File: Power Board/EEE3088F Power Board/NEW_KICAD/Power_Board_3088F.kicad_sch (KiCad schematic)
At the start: 92 parts, among them J1 Conn_02x16_Odd_Even, J2 USB_C_Receptacle, J3 Conn_01x02_Socket, Q1 2N7002, U1 INA219AIDCNR, U10 DRV8837DSGR, U11 DRV8837DSGR, U12 DRV8837DSGR, U13 DRV8837DSGR, U2 TPS5430DDA, U3 TP4056-42-ESOP8, U7 AP22966DC8-7, U9 CH224K

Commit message: finished schematic
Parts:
- removed C_B1, C_B2: 10uF, Capacitor_SMD:C_0603_1608Metric_Pad1.08x0.95mm_HandSolder, symbol Device:C
- removed C_B3: 220uF, Capacitor_SMD:CP_Elec_6.3x7.7, symbol Device:C_Small
- removed C_Bboot1: 10nF, Capacitor_SMD:C_0603_1608Metric_Pad1.08x0.95mm_HandSolder, symbol Device:C_Small
- removed C_Bin1: 10uF, Capacitor_SMD:C_1206_3216Metric_Pad1.33x1.80mm_HandSolder, symbol Device:C_Small
- removed D2: Red LED, LED_SMD:LED_0603_1608Metric_Pad1.05x0.95mm_HandSolder, symbol Device:LED
- removed D3: Green LED, LED_SMD:LED_0805_2012Metric_Pad1.15x1.40mm_HandSolder, symbol Device:LED
- removed D4: BA340A, custom_footprints:SMA-DIODE, symbol Custom_symbols:B340A
- removed J2: USB_C_Receptacle, Connector_USB:USB_C_Receptacle_G-Switch_GT-USB-7010ASV, symbol Connector:USB_C_Receptacle
- removed L1: 18uH, Inductor_SMD:L_Abracon_ASPI-4030S, symbol Device:L_Small
- removed Q1: 2N7002, Package_TO_SOT_SMD:SOT-23, symbol Transistor_FET:2N7002
- removed R19, R20: 1R, Resistor_SMD:R_0603_1608Metric_Pad0.98x0.95mm_HandSolder, symbol Device:R_US
- removed R_B_LED1, R_B_LED2: 1k, Resistor_SMD:R_0603_1608Metric_Pad0.98x0.95mm_HandSolder, symbol Device:R_US
- removed R_B_b1: 100R, Resistor_SMD:R_0603_1608Metric_Pad0.98x0.95mm_HandSolder, symbol Device:R_US
- removed R_B_fast1: 2k7, Resistor_SMD:R_0603_1608Metric_Pad0.98x0.95mm_HandSolder, symbol Device:R_US
- removed R_B_pd1: 10k, Resistor_SMD:R_0603_1608Metric_Pad0.98x0.95mm_HandSolder, symbol Device:R_US
- removed R_B_slow1: 5k6, Resistor_SMD:R_0603_1608Metric_Pad0.98x0.95mm_HandSolder, symbol Device:R_US
- removed R_Bset1: 10k, Resistor_SMD:R_0603_1608Metric_Pad0.98x0.95mm_HandSolder, symbol Device:R_Small_US
- removed R_Bset2: 3k3, Resistor_SMD:R_0603_1608Metric_Pad0.98x0.95mm_HandSolder, symbol Device:R_Small_US
- removed TP10, TP11, TP12, TP13, TP14, TP15, TP17: TestPoint, TestPoint:TestPoint_Pad_D2.0mm, symbol Connector:TestPoint
- removed U1: INA219AIDCNR, Package_TO_SOT_SMD:SOT-23-8, symbol Sensor_Energy:INA219AxDCN
- removed U10, U11, U12, U13: DRV8837DSGR, custom_footprints:SON50P200X200X80-9N, symbol Custom_symbols:DRV8837DSGR
- removed U2: TPS5430DDA, Package_SO:SOIC-8-1EP_3.9x4.9mm_P1.27mm_EP2.29x3mm, symbol Regulator_Switching:TPS5430DDA
- removed U3: TP4056-42-ESOP8, custom_footprints:SOIC127P600X175-9N, symbol Battery_Management:TP4056-42-ESOP8
- added C_B3, C_B5: 10uF, Capacitor_SMD:C_0603_1608Metric_Pad1.08x0.95mm_HandSolder, symbol Device:C
- added C_B4: 220uF, Capacitor_SMD:CP_Elec_6.3x7.7, symbol Device:C_Small
- added C_Bboot2: 10nF, Capacitor_SMD:C_0603_1608Metric_Pad1.08x0.95mm_HandSolder, symbol Device:C_Small
- added C_Bin2: 10uF, Capacitor_SMD:C_1206_3216Metric_Pad1.33x1.80mm_HandSolder, symbol Device:C_Small
- added D4: Red LED, LED_SMD:LED_0603_1608Metric_Pad1.05x0.95mm_HandSolder, symbol Device:LED
- added D7: BA340A, custom_footprints:SMA-DIODE, symbol Custom_symbols:B340A
- added D8: Green LED, LED_SMD:LED_0603_1608Metric_Pad1.05x0.95mm_HandSolder, symbol Device:LED
- added JP_B1: charge_in, Jumper:SolderJumper-2_P1.3mm_Open_RoundedPad1.0x1.5mm, symbol Jumper:SolderJumper_2_Open
- added JP_B2: buck_charge, Jumper:SolderJumper-2_P1.3mm_Open_RoundedPad1.0x1.5mm, symbol Jumper:SolderJumper_2_Open
- added JP_BBatt1: charge_batt+, Jumper:SolderJumper-2_P1.3mm_Open_RoundedPad1.0x1.5mm, symbol Jumper:SolderJumper_2_Open
- added JP_B_ena1: Jumper (leave open), Jumper:SolderJumper-2_P1.3mm_Open_RoundedPad1.0x1.5mm, symbol Jumper:SolderJumper_2_Open
- added JP_Bprog1: fast_prog, Jumper:SolderJumper-2_P1.3mm_Open_RoundedPad1.0x1.5mm, symbol Jumper:SolderJumper_2_Open
- added JP_CVbus1: VBUS, Jumper:SolderJumper-2_P1.3mm_Open_RoundedPad1.0x1.5mm, symbol Jumper:SolderJumper_2_Open
- added JP_M_VM1: Batt_VM, Jumper:SolderJumper-2_P1.3mm_Open_RoundedPad1.0x1.5mm, symbol Jumper:SolderJumper_2_Open
- added JP_P1: Boost_ENA, Jumper:SolderJumper-2_P1.3mm_Open_RoundedPad1.0x1.5mm, symbol Jumper:SolderJumper_2_Open
- added L2: 18uH, Inductor_SMD:L_Abracon_ASPI-4030S, symbol Device:L_Small
- added Q2: 2N7002, Package_TO_SOT_SMD:SOT-23, symbol Transistor_FET:2N7002
- added R21, R22: 1R, Resistor_SMD:R_0603_1608Metric_Pad0.98x0.95mm_HandSolder, symbol Device:R_US
- added R_B_LED3, R_B_LED4: 1k, Resistor_SMD:R_0603_1608Metric_Pad0.98x0.95mm_HandSolder, symbol Device:R_US
- added R_B_b2: 100R, Resistor_SMD:R_0603_1608Metric_Pad0.98x0.95mm_HandSolder, symbol Device:R_US
- added R_B_fast2: 2k7, Resistor_SMD:R_0603_1608Metric_Pad0.98x0.95mm_HandSolder, symbol Device:R_US
- added R_B_pd2: 10k, Resistor_SMD:R_0603_1608Metric_Pad0.98x0.95mm_HandSolder, symbol Device:R_US
- added R_B_slow2: 5k6, Resistor_SMD:R_0603_1608Metric_Pad0.98x0.95mm_HandSolder, symbol Device:R_US
- added R_Bset3: 10k, Resistor_SMD:R_0603_1608Metric_Pad0.98x0.95mm_HandSolder, symbol Device:R_Small_US
- added R_Bset4: 3k3, Resistor_SMD:R_0603_1608Metric_Pad0.98x0.95mm_HandSolder, symbol Device:R_Small_US
- added TP_B1, TP_B_Drain3, TP_B_Gate1, TP_B_sense1, TP_MA2, TP_MB2: TestPoint, TestPoint:TestPoint_Pad_D2.0mm, symbol Connector:TestPoint
- added TP_B_prog1: charge_prog, TestPoint:TestPoint_Pad_D2.0mm, symbol Connector:TestPoint
- added TP_B_prog2: charge_gnd, TestPoint:TestPoint_Pad_D2.0mm, symbol Connector:TestPoint
- added TP_GND0: GND_REF, TestPoint:TestPoint_Pad_D2.0mm, symbol Connector:TestPoint
- added U14, U15, U16, U17: DRV8837DSGR, custom_footprints:SON50P200X200X80-9N, symbol Custom_symbols:DRV8837DSGR
- added U2: INA219AxDCN, Package_TO_SOT_SMD:SOT-23-8, symbol Sensor_Energy:INA219AxDCN
- added U4: ~, custom_footprints:USB-C-SMD_G-SWITCH_GT-USB-7010ASV, symbol Custom_symbols:GT-USB-7010ASV
- added U5: TPS5430DDA, Package_SO:SOIC-8-1EP_3.9x4.9mm_P1.27mm_EP2.29x3mm, symbol Regulator_Switching:TPS5430DDA
- added U6: TP4056-42-ESOP8, custom_footprints:SOIC127P600X175-9N, symbol Battery_Management:TP4056-42-ESOP8
- 3V3: renamed from D6; footprint LED_SMD:LED_0805_2012Metric_Pad1.15x1.40mm_HandSolder -> LED_SMD:LED_0603_1608Metric_Pad1.05x0.95mm_HandSolder
- 5V0: renamed from D5; footprint LED_SMD:LED_0805_2012Metric_Pad1.15x1.40mm_HandSolder -> LED_SMD:LED_0603_1608Metric_Pad1.05x0.95mm_HandSolder
- renumbered JPI3 to JPI_3, JPI2 to JP_I1, JPI1 to JP_I2, JPI6 to JP_L1, JPI4 to JP_L2, JPI5 to JP_L3, JP_P1 to JP_P3, JP_P3 to JP_P4, TP_P6 to TP_3V3, TP_P3 to TP_5V0, TP19 to TP_L1, TP18 to TP_L2, TP_P1 to TP_PA1, TP_P2 to TP_PA2, TP_P4 to TP_PB1, TP_P5 to TP_PB2
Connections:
- net -BATT is gone; now on net GND: Batt-1.1, J3.2 (Pin_2)
- net Batt+ is gone; now on net +BATT: JPI_3.1 (A), R_Ishunt1.2
- net +3.3V: now also C_P(in)2.2, R_P2.1, TP_3V3.1, U_P2.2 (VO)
- net +9V: now also JP_B1.2 (B), JP_CVbus1.1 (A)
- net +BATT: now also J1.14 (Pin_14), U2.2 (IN-)
- net 3V3_M: now also U14.7 (~{SLEEP}), U14.8 (VCC), U15.7 (~{SLEEP}), U15.8 (VCC), U16.7 (~{SLEEP}), U16.8 (VCC), U17.7 (~{SLEEP}), U17.8 (VCC)
- net 5V_Buck_Out: now also JP_B2.1 (A), R21.1, R22.1
- net Battery: now also JP_BBatt1.2 (B), JP_M_VM1.1 (A), U2.1 (IN+); no longer J1.14 (Pin_14)
- net CC1: now also U4.A5 (CC1)
- net CC2: now also U4.B5 (CC2)
- net D+: now also U4.A6 (DP1), U4.B6 (DP2)
- net D-: now also U4.A7 (DN1), U4.B7 (DN2)
- net FAST_CHARGE_CTRL: now also R_B_b2.1, TP_B1.1
- net GND: now also C_B3.2, C_B4.2, C_B5.2, C_Bin2.2, D7.A, JP_B_ena1.1 (A), Q2.2 (S), R_B_pd2.2, R_B_slow2.2, R_Bset4.2, TP_B_prog2.1, TP_GND0.1, U14.4 (GND), U14.9 (EXP), U15.4 (GND), U15.9 (EXP), U16.4 (GND), U16.9 (EXP), U17.4 (GND), U17.9 (EXP), U4.1 (SHELL), U4.2 (SHELL), U4.3 (SHELL), U4.4 (SHELL), U4.A1B12 (GND), U4.B1A12 (GND), U5.6 (GND), U5.9 (GNDPAD), U6.1 (TEMP), U6.3 (GND)
- net I2C1_SCL: now also U2.5 (SCL), U2.8 (A1)
- net I2C1_SDA: now also U2.6 (SDA)
- net MOTOR1_A_OUT: now also U15.2 (OUT1)
- net MOTOR1_B_OUT: now also U15.3 (OUT2)
- net MOTOR1_CTRL1: now also U15.6 (IN1)
- net MOTOR1_CTRL2: now also U15.5 (IN2)
- net MOTOR2_A_OUT: now also TP_MA2.1, U14.2 (OUT1)
- net MOTOR2_B_OUT: now also TP_MB2.1, U14.3 (OUT2)
- net MOTOR2_CTRL1: now also U14.6 (IN1)
- net MOTOR2_CTRL2: now also U14.5 (IN2)
- net MOTOR3_A_OUT: now also U17.2 (OUT1)
- net MOTOR3_B_OUT: now also U17.3 (OUT2)
- net MOTOR3_CTRL1: now also U17.6 (IN1)
- net MOTOR3_CTRL2: now also U17.5 (IN2)
- net MOTOR4_A_OUT: now also U16.2 (OUT1)
- net MOTOR4_B_OUT: now also U16.3 (OUT2)
- net MOTOR4_CTRL1: now also U16.6 (IN1)
- net MOTOR4_CTRL2: now also U16.5 (IN2)
- net at C_P(in)3.2, JP_P2.2 (B), JP_P3.1 (A)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: now also JP_P1.1 (A); no longer U_P1.5 (EN)
- net at C_I(in)1.2, JP_I1.2 (B): now also U2.4 (VS)
- new net: D4.1 (K), R_B_LED3.1
- new net: C_B3.1, D4.2 (A), D8.2 (A), R21.2, R22.2, U6.4 (V_{CC}), U6.8 (CE)
- new net: Q2.1 (G), R_B_b2.2, R_B_pd2.1, TP_B_Gate1.1
- new net: JP_B_ena1.2 (B), U6.9 (EPAD)
- new net: R_Bset3.2, R_Bset4.1, TP_B_sense1.1, U5.4 (VSENSE)
- new net: JP_Bprog1.1 (A), R_B_slow2.1, TP_B_prog1.1, U6.2 (PROG)
- new net: C_B5.1, JP_BBatt1.1 (A), U6.5 (BAT)
- new net: R_B_LED3.2, U6.6 (~{STDBY})
- new net: R_B_LED4.2, U6.7 (~{CHRG})
- new net: Q2.3 (D), R_B_fast2.2, TP_B_Drain3.1
- new net: JP_P1.2 (B), U_P1.5 (EN)
- new net: D8.1 (K), R_B_LED4.1
- new net: C_B4.1, JP_B2.2 (B), L2.2, R_Bset3.1
- new net: C_Bboot2.2, D7.C, L2.1, U5.8 (PH)
- new net: C_Bboot2.1, U5.1 (BOOT)
- new net: C_Bin2.1, JP_B1.1 (A), U5.7 (VIN)
- new net: JP_Bprog1.2 (B), R_B_fast2.1
- new net: JP_CVbus1.2 (B), U4.A4B9 (VBUS), U4.B4A9 (VBUS)
- new net: U2.3 (GND), U2.7 (A0)
- new net Battery_VM: JP_M_VM1.2 (B), U14.1 (VM), U15.1 (VM), U16.1 (VM), U17.1 (VM)
- no-connect marks 20 -> 11
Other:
- note added: "Acceptance testing: - test 9V supply / connect 9V supply - solder JP_B1 - test buck out =5V - solder JP_B2 - test R_B_slow - test VBAT (JP_BBatt1) - soler JP_BBatt1 - check slow charging current - solder JP_Bprog1 - test switching 2N7002 - test fast charging using switching"
- note added: "battery terminal"
- note added: "circuit side"
- note added: "leave jumper open to enable (float) solder to disable"
- note removed: "**fix footprint"
- note removed: "Done: - Resistors and Capacitors footprints (except LM256) - IC footprints - Schottky diode and 2N7002 footprints - LED footprints To Do: - LM256 caps and inductor? - ask about 0.4R resistor - Neaten net labels - relabel passive components"
- note removed: "To Do list in a suggestive order: 1) Clarity on our design assumptions 2) Check all design logic (esp Volt reg values), check eachothers Add testing procedure comments and test points. 3) Assign footprints (check with eachother as we go. This is the biggest killer of PCBs. This includes passives and ensuring basic passives available on JLC Have chats with others abt plugin and finding footprints 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"
- note removed: "add P MOSFET between Vbus and HV?"
- note removed: "jump"
- note removed: "jump 3V3 Out jump +Batt"
- note removed: "jump each IC?"
- moved on the sheet: 3V3, 5V0, Batt+1, Batt-1, C_C_dd1, C_P(in)1, C_P(in)2, C_P(in)3, C_P(out)1, C_P(out)2, C_P(out)3, J1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

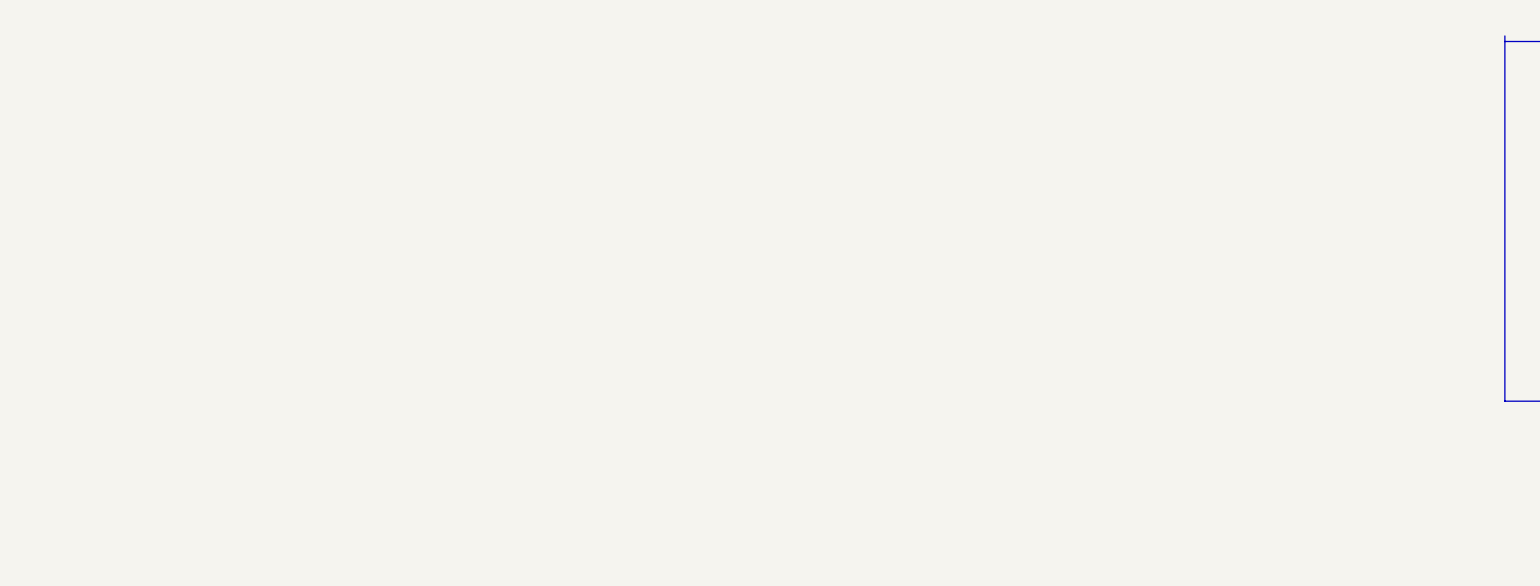
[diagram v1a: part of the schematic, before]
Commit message: pcb islands done
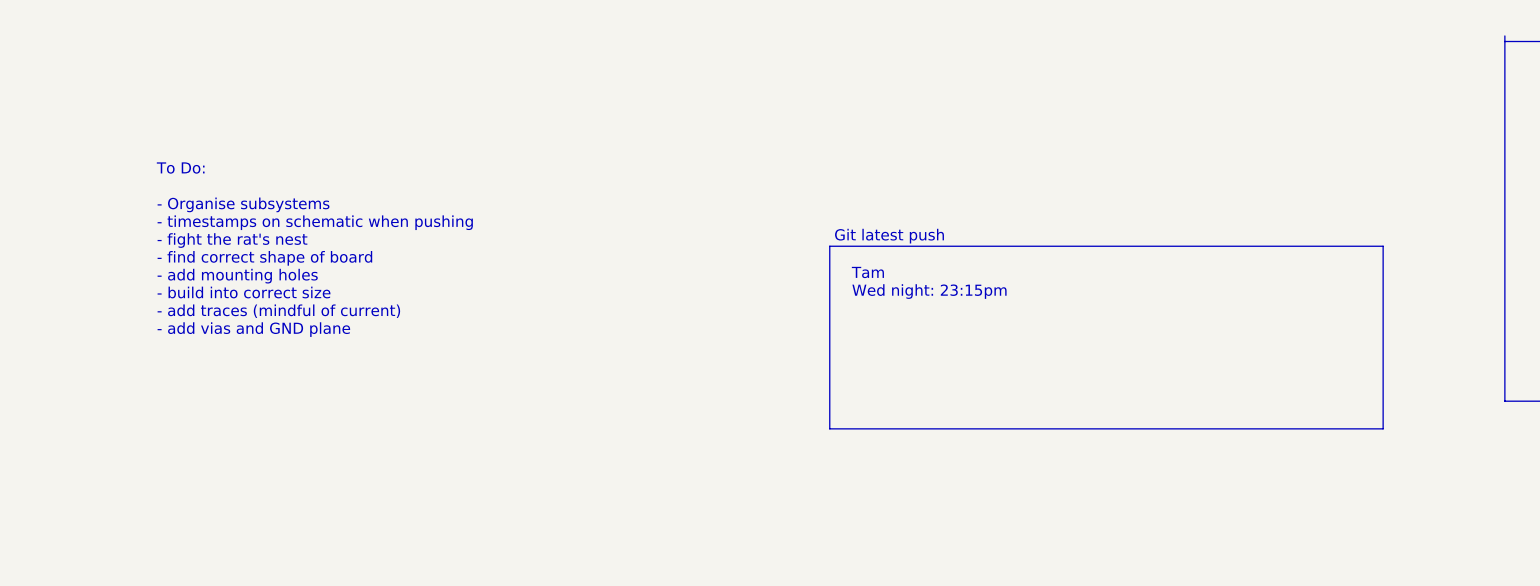
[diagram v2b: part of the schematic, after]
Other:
- note added: "Git latest push"
- note added: "Tam Wed night: 23:15pm"
- note added: "To Do: - Organise subsystems - timestamps on schematic when pushing - fight the rat's nest - find correct shape of board - add mounting holes - build into correct size - add traces (mindful of current) - add vias and GND plane"
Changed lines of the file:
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@@
+		)
+	)
+	(text "Git latest push"
+		(exclude_from_sim no)
+		(at 413.258 348.234 0)
+		(effects
+			(font
+				(size 1.27 1.27)
+			)
+			(justify left)
+		)
+	)
+	(text "To Do:\n\n- Organise subsystems\n- timestamps on schematic when pushing\n- fight the rat's nest\n- find correct shape of board\n- add mounting holes\n- build into correct size\n- add traces (mindful of current)\n- add vias and GND plane"
+		(exclude_from_sim no)
+		(at 335.534 349.758 0)
+		(effects
+			(font
+				(size 1.27 1.27)
+			)
+			(justify left)
 		)
 	)
@@
 		)
 	)
+	(text "Tam\nWed night: 23:15pm"
+		(exclude_from_sim no)
+		(at 415.29 353.568 0)
+		(effects
+			(font
+				(size 1.27 1.27)
+			)
+			(justify left)
+		)
+	)
 	(text "test points?"
 		(exclude_from_sim no)
@@
 		)
 	)
+	(polyline
+		(pts
+			(xy 412.75 349.25) (xy 476.25 349.25)
+		)
+		(stroke
+			(width 0)
+			(type default)
+		)
+	)
 	(wire
 		(pts
@@
 		)
 	)
+	(polyline
+		(pts
+			(xy 412.75 370.205) (xy 476.25 370.205)
+		)
+		(stroke
+			(width 0)
+			(type default)
+		)
+	)
 	(wire
 		(pts
@@
 		)
 	)
+	(polyline
+		(pts
+			(xy 412.75 349.25) (xy 412.75 370.205)
+		)
+		(stroke
+			(width 0)
+			(type default)
+		)
+	)
 	(wire
 		(pts
@@
 		)
 		(stroke
+			(width 0)
+			(type default)
+		)
+	)
+	(polyline
+		(pts
+			(xy 476.25 370.205) (xy 476.25 349.25)
+		)
+		(stroke

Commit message: arranged rats nest Tam
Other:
- note added: "Tam thurs 9:50am"
- note removed: "Tam Wed night: 23:15pm"
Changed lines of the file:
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@@
 		)
 	)
-	(text "Tam\nWed night: 23:15pm"
+	(text "Tam\nthurs 9:50am"
 		(exclude_from_sim no)
 		(at 415.29 353.568 0)

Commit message: Glen finished organising PCB & some 3D
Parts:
- removed TP21: TestPoint, TestPoint:TestPoint_Pad_D2.0mm, symbol Connector:TestPoint
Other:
- note added: "Deleted redundant TP"
- note added: "Tam thurs 9:50am Glen: 12:28"
- note removed: "Tam thurs 9:50am"
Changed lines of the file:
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@@
 		)
 	)
+	(text "Deleted redundant TP"
+		(exclude_from_sim no)
+		(at 115.316 244.094 0)
+		(effects
+			(font
+				(size 1.27 1.27)
+			)
+		)
+	)
 	(text "must still determine which inductor. REQ:\nValue = 1u\nLow Sat current\nDCR"
 		(exclude_from_sim no)
@@
 		)
 	)
-	(text "Tam\nthurs 9:50am"
+	(text "Tam\nthurs 9:50am\nGlen: 12:28"
 		(exclude_from_sim no)
 		(at 415.29 353.568 0)
@@
 	)
 	(junction
-		(at 101.6 245.11)
-		(diameter 0)
-		(color 0 0 0 0)
-	)
-	(junction
 		(at 264.16 308.61)
 		(diameter 0)
@@
 	(wire
 		(pts
-			(xy 101.6 245.11) (xy 109.22 245.11)
-		)
-		(stroke
-			(width 0)
-			(type default)
-		)
-	)
-	(wire
-		(pts
 			(xy 152.4 57.15) (xy 160.02 57.15)
 		)
@@
 					(unit 1)
 				)
-			)
-		)
-	)
-	(symbol
-		(lib_id "Connector:TestPoint")
-		(at 109.22 245.11 0)
-		(unit 1)
-		(exclude_from_sim no)
-		(in_bom yes)
-		(on_board yes)
-		(dnp no)
-		(fields_autoplaced yes)
-		(property "Reference" "TP21"
-			(at 111.76 240.5379 0)
-			(effects
-				(font
-					(size 1.27 1.27)
-				)
-				(justify left)
-			)
-		)
-		(property "Value" "TestPoint"
-			(at 111.76 243.0779 0)
-			(effects
-				(font
-					(size 1.27 1.27)
-				)
-				(justify left)
-			)
-		)
-		(property "Footprint" "TestPoint:TestPoint_Pad_D2.0mm"
-			(at 114.3 245.11 0)
-			(effects
-				(font
-					(size 1.27 1.27)
-				)
-				(hide yes)
-			)
-		)
-		(property "Datasheet" "~"
-			(at 114.3 245.11 0)
-			(effects
-				(font
-					(size 1.27 1.27)
-				)
-				(hide yes)
-			)
-		)
-		(property "Description" "test point"
-			(at 109.22 245.11 0)
-			(effects
-				(font
-					(size 1.27 1.27)
-				)
-				(hide yes)
-			)
-		)
-		(pin "1"
-		)
-		(instances
-			(project "Power_Board_3088F"
-				(path "/5c7d371d-807a-42c2-8c94-eee361c0fe38"
-					(reference "TP21")
-					(unit 1)
-				)

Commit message: traces started
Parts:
- added H1: MountingHole, MountingHole:MountingHole_3.2mm_M3, symbol Mechanical:MountingHole
- renumbered TP6 to 9V1, Batt+1 to B+1, Batt-1 to B-1, TP_B_sense1 to BS1, TP_B_Drain3 to B_D3, TP_B_Gate1 to B_G1, TP_B_prog1 to B_prog1, TP_B_prog2 to B_prog2, JP_B1 to Bin1, TP9 to CFG1, C_Bin2 to C_B1, C_Bboot2 to C_B2, C_C_dd1 to C_C1, C15 to C_L1, C25 to C_L2, C16 to C_L3, C17 to C_L4, C_P(in)3 to C_P1, C_P(out)1 to C_P2, C_P(out)2 to C_P3, C_P(out)3 to C_P4, C_P(in)1 to C_P5, C_P(in)2 to C_P6, TP_GND0 to GND0, TP8 to GND1, JP_I1 to J_I1, JP_I2 to J_I2, JPI_3 to J_I3, JP_L2 to J_L2, JP_L1 to J_L3, JP_L3 to L3, L2 to LB1, L3 to L_P3, TP_MA2 to MA2, TP_MB2 to MB2, JP_M_3V3 to M_3V3, JP_M_VM1 to M_VM1, JP_P1 to P1, JP_P2 to P2, JP_P3 to P3, JP_P4 to P4, TP_PA1 to PA1, TP_PA2 to PA2, TP_PB1 to PB1, TP_PB2 to PB2, R_Bset3 to R_B1, R_Bset4 to R_B2, R_B_LED3 to R_B3, R_B_LED4 to R_B4, R_B_b2 to R_B6, R_B_pd2 to R_B7, R_B_fast2 to R_Bfast1, R_B_slow2 to R_Bslow2, R_C_bus1 to R_C1, R_C_dd1 to R_C2, R_C_cfg1 to R_C3, R_Ishunt1 to R_SH1, TP_3V3 to T_3V3, TP_L1 to T_L1, TP_L2 to T_L2, TP7 to VDD1, JP_CVbus1 to Vbus_9
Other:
- note added: "Tam thurs 9:50am Glen: 12:28 Tam: 18:10pm"
- note removed: "Tam thurs 9:50am Glen: 12:28"

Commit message: Mostly finished Schem
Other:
- note added: "Tam thurs 9:50am Glen: 12:28 Tam: 18:10pm Glen: 21:39"
- note removed: "Tam thurs 9:50am Glen: 12:28 Tam: 18:10pm"
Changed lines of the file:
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@@
 		)
 	)
-	(text "Tam\nthurs 9:50am\nGlen: 12:28\nTam: 18:10pm"
+	(text "Tam\nthurs 9:50am\nGlen: 12:28\nTam: 18:10pm\nGlen: 21:39"
 		(exclude_from_sim no)
 		(at 415.036 354.838 0)

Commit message: final v0
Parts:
- D7: footprint custom_footprints:SMA-DIODE -> custom_footprints:B340A; LCSC Part Name (none) -> 电压:40V 电流:3A; Manufacturer (none) -> MDD(辰达半导体); Manufacturer Part (none) -> B340A; Supplier (none) -> LCSC; Supplier Part (none) -> C64982
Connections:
- net GND: now also D7.2 (A); no longer D7.A
- net at C_B2.2, LB1.1, U5.8 (PH): now also D7.1 (K); no longer D7.C
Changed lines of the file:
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@@
 	(text "B340A"
 		(exclude_from_sim no)
-		(at 387.858 214.122 0)
+		(at 387.096 216.154 0)
 		(effects
 			(font
@@
 	)
 	(junction
+		(at 382.27 219.71)
+		(diameter 0)
+		(color 0 0 0 0)
+	)
+	(junction
 		(at 85.09 57.15)
 		(diameter 0)
@@
 		(color 0 0 0 0)
 	)
-	(junction
-		(at 382.27 215.9)
-		(diameter 0)
-		(color 0 0 0 0)
-	)
 	(no_connect
 		(at 257.81 215.9)
@@
 	(wire
 		(pts
-			(xy 400.05 214.63) (xy 400.05 215.9)
+			(xy 400.05 214.63) (xy 400.05 218.44)
 		)
 		(stroke
@@
 	(wire
 		(pts
+			(xy 382.27 209.55) (xy 382.27 208.28)
+		)
+		(stroke
+			(width 0)
+			(type default)
+		)
+	)
+	(wire
+		(pts
 			(xy 471.17 283.21) (xy 483.87 283.21)
 		)
@@
 	(wire
 		(pts
-			(xy 400.05 215.9) (xy 382.27 215.9)
+			(xy 400.05 218.44) (xy 382.27 218.44)
 		)
 		(stroke
@@
 	(wire
 		(pts
-			(xy 382.27 208.28) (xy 382.27 209.55)
-		)
-		(stroke
-			(width 0)
-			(type default)
-		)
-	)
-	(wire
-		(pts
 			(xy 229.87 241.3) (xy 245.11 241.3)
 		)
@@
 	(wire
 		(pts
+			(xy 382.27 219.71) (xy 382.27 218.44)
+		)
+		(stroke
+			(width 0)
+			(type default)
+		)
+	)
+	(wire
+		(pts
 			(xy 50.8 180.34) (xy 66.04 180.34)
 		)
@@
 	(wire
 		(pts
-			(xy 382.27 214.63) (xy 382.27 215.9)
-		)
-		(stroke
-			(width 0)
-			(type default)
-		)
-	)
-	(wire
-		(pts
 			(xy 102.87 162.56) (xy 102.87 165.1)
 		)
@@
 	(symbol
 		(lib_id "power:GND")
-		(at 382.27 215.9 0)
+		(at 382.27 219.71 0)
 		(unit 1)
 		(exclude_from_sim no)
@@
 		(fields_autoplaced yes)
 		(property "Reference" "#PWR059"
-			(at 382.27 222.25 0)
+			(at 382.27 226.06 0)
 			(effects
 				(font
@@
 		)
 		(property "Value" "GND"
-			(at 382.27 220.98 0)
+			(at 382.27 224.79 0)
 			(effects
 				(font
@@
 		)
 		(property "Footprint" ""
-			(at 382.27 215.9 0)
+			(at 382.27 219.71 0)
 			(effects
 				(font
@@
 		)
 		(property "Datasheet" ""
-			(at 382.27 215.9 0)
+			(at 382.27 219.71 0)
 			(effects
 				(font
@@
 		)
 		(property "Description" "Power symbol creates a global label with name \"GND\" , ground"
-			(at 382.27 215.9 0)
+			(at 382.27 219.71 0)
 			(effects
 				(font
@@
 	(symbol
 		(lib_id "Custom_symbols:B340A")
-		(at 382.27 212.09 90)
+		(at 382.27 214.63 270)
 		(unit 1)
 		(exclude_from_sim no)
@@
 		(fields_autoplaced yes)
 		(property "Reference" "D7"
-			(at 384.81 211.8359 90)
+			(at 384.81 214.2489 90)
 			(effects
 				(font
 					(size 1.27 1.27)
 				)
-				(justify right)
+				(justify left)
 			)
 		)
 		(property "Value" "BA340A"
-			(at 382.27 212.09 0)
+			(at 382.27 214.63 0)
 			(effects
 				(font
@@
 			)
 		)
-		(property "Footprint" "custom_footprints:SMA-DIODE"
-			(at 382.27 212.09 0)
+		(property "Footprint" "custom_footprints:B340A"
+			(at 382.27 214.63 0)
 			(effects
 				(font
 					(size 1.27 1.27)
 				)
-				(justify bottom)
 				(hide yes)
 			)
 		)
-		(property "Datasheet" ""
-			(at 382.27 212.09 0)
+		(property "Datasheet" "https://atta.szlcsc.com/upload/public/pdf/source/20240710/591710C3B34CDB7FE3DA92C119E6F598.pdf"
+			(at 382.27 214.63 0)
 			(effects
 				(font
@@
 			)
 		)
-		(property "Description" ""
-			(at 382.27 212.09 0)
+		(property "Description" "Diode Configuration:Independent Type Forward Voltage (Vf@If):550mV@3A Reverse Voltage (Vr):40V Rectified Current:3A Reverse Leakage Current (Ir):500uA@40V"
+			(at 382.27 214.63 0)
 			(effects
 				(font
@@
 		)
 		(property "MF" "Diodes Zetex"
-			(at 382.27 212.09 0)
+			(at 382.27 214.63 0)
 			(effects
 				(font
@@
 		)
 		(property "Description_1" "Rectifier Diode Schottky 40V 3A 2-Pin SMA T/R"
-			(at 382.27 212.09 0)
+			(at 382.27 214.63 0)
 			(effects
 				(font
@@
 		)
 		(property "Package" "None"
-			(at 382.27 212.09 0)
+			(at 382.27 214.63 0)
 			(effects
 				(font
@@
 		)
 		(property "Price" "None"
-			(at 382.27 212.09 0)
+			(at 382.27 214.63 0)
 			(effects
 				(font
@@
 		)
 		(property "Check_prices" "https://www.snapeda.com/parts/B340A/Diodes+Inc./view-part/?ref=eda"
-			(at 382.27 212.09 0)
+			(at 382.27 214.63 0)
 			(effects
 				(font
@@
 		)
 		(property "PROD_ID" "DIO-09886"
-			(at 382.27 212.09 0)
+			(at 382.27 214.63 0)
 			(effects
 				(font
@@
 		)
 		(property "SnapEDA_Link" "https://www.snapeda.com/parts/B340A/Diodes+Inc./view-part/?ref=snap"
-			(at 382.27 212.09 0)
+			(at 382.27 214.63 0)
 			(effects
 				(font
@@
 		)
 		(property "Availability" "In Stock"
-			(at 382.27 212.09 0)
+			(at 382.27 214.63 0)
 			(effects
 				(font
@@
 		)
 		(property "MP" "B340A"
-			(at 382.27 212.09 0)
+			(at 382.27 214.63 0)
 			(effects
 				(font
@@
 			)
 		)
-		(pin "A"
+		(property "Manufacturer Part" "B340A"
+			(at 382.27 214.63 0)
+			(effects
+				(font
+					(size 1.27 1.27)
+				)
+				(hide yes)
+			)
 		)
-		(pin "C"
+		(property "Manufacturer" "MDD(辰达半导体)"
+			(at 382.27 214.63 0)
+			(effects
+				(font
+					(size 1.27 1.27)
+				)
+				(hide yes)
+			)
+		)
+		(property "Supplier Part" "C64982"
+			(at 382.27 214.63 0)
+			(effects
+				(font
+					(size 1.27 1.27)
+				)
+				(hide yes)
+			)
+		)
+		(property "Supplier" "LCSC"
+			(at 382.27 214.63 0)
+			(effects
+				(font
+					(size 1.27 1.27)
+				)
+				(hide yes)
+			)
+		)
+		(property "LCSC Part Name" "电压:40V 电流:3A"
+			(at 382.27 214.63 0)
+			(effects
+				(font
+					(size 1.27 1.27)
+				)
+				(hide yes)
+			)
+		)
+		(pin "1"
+		)
+		(pin "2"
 		)
 		(instances
